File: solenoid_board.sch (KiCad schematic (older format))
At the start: 30 parts, among them J2 MCU_LEFT_LEGS, J3 MCU_RIGHT_LEGS

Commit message: Changed resistor footprints, changed resistor supplier. Still need to route wires.
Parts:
- R330, R331, R332, R333, R334, R335, R336, R337, R338: footprint Resistor_SMD:R_2010_5025Metric_Pad1.52x2.65mm_HandSolder -> Resistor_THT:R_Axial_DIN0309_L9.0mm_D3.2mm_P20.32mm_Horizontal
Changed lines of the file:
@@
 F 0 "R330" V 9000 850 50  0000 C CNN
 F 1 "330" V 9016 850 50  0001 C CNN
-F 2 "Resistor_SMD:R_2010_5025Metric_Pad1.52x2.65mm_HandSolder" V 8830 850 50  0001 C CNN
+F 2 "Resistor_THT:R_Axial_DIN0309_L9.0mm_D3.2mm_P20.32mm_Horizontal" V 8830 850 50  0001 C CNN
 F 3 "~" H 8900 850 50  0001 C CNN
 	1    8900 850
@@
 F 0 "R331" V 9000 1100 50  0000 C CNN
 F 1 "330" V 9016 1100 50  0001 C CNN
-F 2 "Resistor_SMD:R_2010_5025Metric_Pad1.52x2.65mm_HandSolder" V 8830 1100 50  0001 C CNN
+F 2 "Resistor_THT:R_Axial_DIN0309_L9.0mm_D3.2mm_P20.32mm_Horizontal" V 8830 1100 50  0001 C CNN
 F 3 "~" H 8900 1100 50  0001 C CNN
 	1    8900 1100
@@
 F 0 "R332" V 9000 1350 50  0000 C CNN
 F 1 "330" V 9016 1350 50  0001 C CNN
-F 2 "Resistor_SMD:R_2010_5025Metric_Pad1.52x2.65mm_HandSolder" V 8830 1350 50  0001 C CNN
+F 2 "Resistor_THT:R_Axial_DIN0309_L9.0mm_D3.2mm_P20.32mm_Horizontal" V 8830 1350 50  0001 C CNN
 F 3 "~" H 8900 1350 50  0001 C CNN
 	1    8900 1350
@@
 F 0 "R333" V 9000 1600 50  0000 C CNN
 F 1 "R" V 9016 1600 50  0001 C CNN
-F 2 "Resistor_SMD:R_2010_5025Metric_Pad1.52x2.65mm_HandSolder" V 8830 1600 50  0001 C CNN
+F 2 "Resistor_THT:R_Axial_DIN0309_L9.0mm_D3.2mm_P20.32mm_Horizontal" V 8830 1600 50  0001 C CNN
 F 3 "~" H 8900 1600 50  0001 C CNN
 	1    8900 1600
@@
 F 0 "R334" V 9000 1850 50  0000 C CNN
 F 1 "R" V 9016 1850 50  0001 C CNN
-F 2 "Resistor_SMD:R_2010_5025Metric_Pad1.52x2.65mm_HandSolder" V 8830 1850 50  0001 C CNN
+F 2 "Resistor_THT:R_Axial_DIN0309_L9.0mm_D3.2mm_P20.32mm_Horizontal" V 8830 1850 50  0001 C CNN
 F 3 "~" H 8900 1850 50  0001 C CNN
 	1    8900 1850
@@
 F 0 "R335" V 9000 2100 50  0000 C CNN
 F 1 "R" V 9016 2100 50  0001 C CNN
-F 2 "Resistor_SMD:R_2010_5025Metric_Pad1.52x2.65mm_HandSolder" V 8830 2100 50  0001 C CNN
+F 2 "Resistor_THT:R_Axial_DIN0309_L9.0mm_D3.2mm_P20.32mm_Horizontal" V 8830 2100 50  0001 C CNN
 F 3 "~" H 8900 2100 50  0001 C CNN
 	1    8900 2100
@@
 F 0 "R336" V 9000 2350 50  0000 C CNN
 F 1 "R" V 9016 2350 50  0001 C CNN
-F 2 "Resistor_SMD:R_2010_5025Metric_Pad1.52x2.65mm_HandSolder" V 8830 2350 50  0001 C CNN
+F 2 "Resistor_THT:R_Axial_DIN0309_L9.0mm_D3.2mm_P20.32mm_Horizontal" V 8830 2350 50  0001 C CNN
 F 3 "~" H 8900 2350 50  0001 C CNN
 	1    8900 2350
@@
 F 0 "R337" V 9000 2600 50  0000 C CNN
 F 1 "R" V 9016 2600 50  0001 C CNN
-F 2 "Resistor_SMD:R_2010_5025Metric_Pad1.52x2.65mm_HandSolder" V 8830 2600 50  0001 C CNN
+F 2 "Resistor_THT:R_Axial_DIN0309_L9.0mm_D3.2mm_P20.32mm_Horizontal" V 8830 2600 50  0001 C CNN
 F 3 "~" H 8900 2600 50  0001 C CNN
 	1    8900 2600
@@
 F 0 "R338" V 9000 2900 50  0000 C CNN
 F 1 "R" V 9016 2900 50  0001 C CNN
-F 2 "Resistor_SMD:R_2010_5025Metric_Pad1.52x2.65mm_HandSolder" V 8830 2900 50  0001 C CNN
+F 2 "Resistor_THT:R_Axial_DIN0309_L9.0mm_D3.2mm_P20.32mm_Horizontal" V 8830 2900 50  0001 C CNN
 F 3 "~" H 8900 2900 50  0001 C CNN
 	1    8900 2900

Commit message: Rearranged Component Geometry, switched out Transciever Resistor footprints, Routed Some wires.
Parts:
- R10, R11: footprint Resistor_SMD:R_2010_5025Metric_Pad1.52x2.65mm_HandSolder -> Resistor_THT:R_Axial_DIN0309_L9.0mm_D3.2mm_P20.32mm_Horizontal
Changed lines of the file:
@@
 F 0 "R11" V 2950 3200 50  0000 C CNN
 F 1 "10" V 2750 3200 50  0001 C CNN
-F 2 "Resistor_SMD:R_2010_5025Metric_Pad1.52x2.65mm_HandSolder" V 2780 3200 50  0001 C CNN
+F 2 "Resistor_THT:R_Axial_DIN0309_L9.0mm_D3.2mm_P20.32mm_Horizontal" V 2780 3200 50  0001 C CNN
 F 3 "~" H 2850 3200 50  0001 C CNN
 	1    2850 3200
@@
 F 0 "R10" V 2750 2950 50  0000 C CNN
 F 1 "10" V 2734 2950 50  0001 C CNN
-F 2 "Resistor_SMD:R_2010_5025Metric_Pad1.52x2.65mm_HandSolder" V 2780 2950 50  0001 C CNN
+F 2 "Resistor_THT:R_Axial_DIN0309_L9.0mm_D3.2mm_P20.32mm_Horizontal" V 2780 2950 50  0001 C CNN
 F 3 "~" H 2850 2950 50  0001 C CNN
 	1    2850 2950

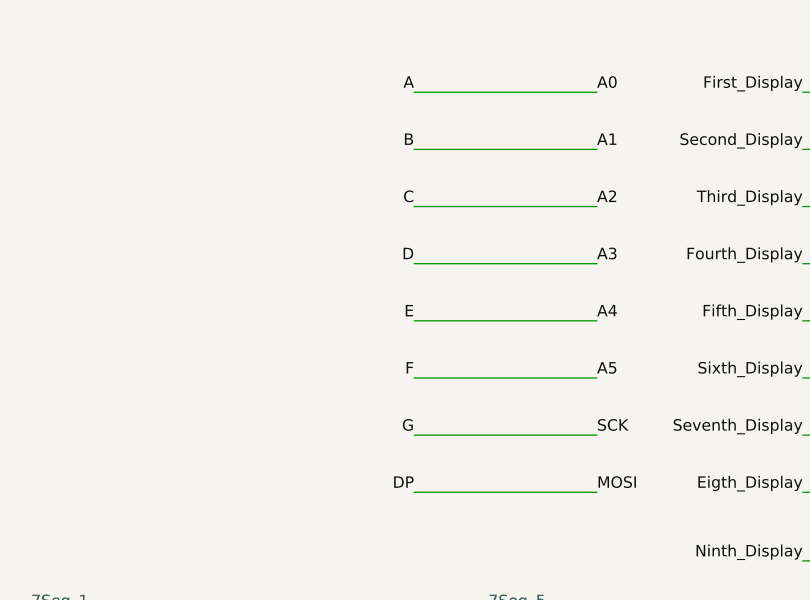
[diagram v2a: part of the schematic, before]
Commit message: Finished Routing and generated new .gbr files. I am unsatisfied with the size of the board, and the geometry may need to be moved around to allow ball count to be displayed underneath the score.
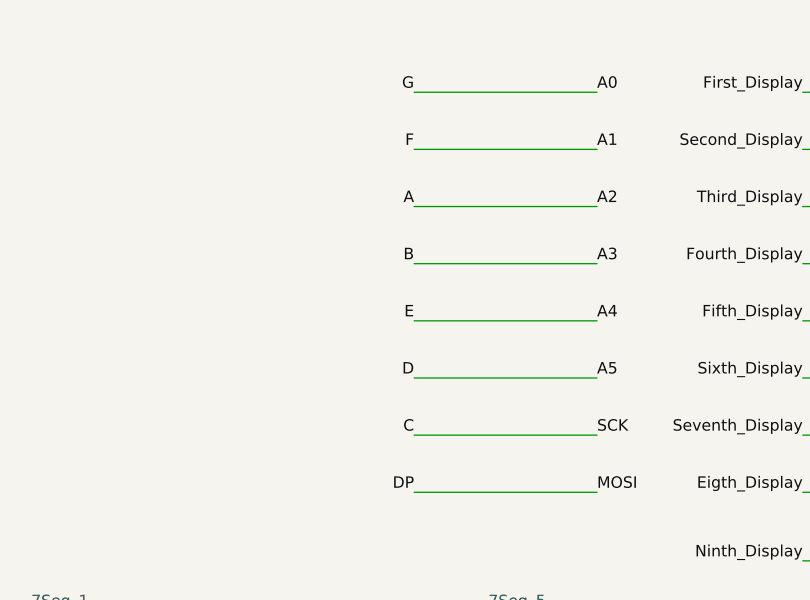
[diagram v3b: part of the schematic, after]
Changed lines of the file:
@@
 Ninth_Display
 Text Label 6800 850  2    50   ~ 0
+G
+Text Label 6800 1100 2    50   ~ 0
+F
+Text Label 6800 1350 2    50   ~ 0
 A
-Text Label 6800 1100 2    50   ~ 0
+Text Label 6800 1600 2    50   ~ 0
 B
-Text Label 6800 1350 2    50   ~ 0
-C
-Text Label 6800 1600 2    50   ~ 0
-D
 Text Label 6800 1850 2    50   ~ 0
 E
 Text Label 6800 2100 2    50   ~ 0
-F
+D
 Text Label 6800 2350 2    50   ~ 0
-G
+C
 Text Label 6800 2600 2    50   ~ 0
 DP

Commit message: Changed BOM, changed Schematic symbols/footprints. Still need to add mosfets and ICs.
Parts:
- removed +5V_IN1: MCU_PWR_Supply, TerminalBlock:TerminalBlock_bornier-2_P5.08mm, symbol Connector:Screw_Terminal_01x02
- removed 7Seg_5, 7Seg_6, 7Seg_7, 7Seg_8, 7Seg_9: Conn_02x05_Top_Bottom, Display_7Segment:7SegmentLED_LTS6760_LTS6780, symbol Connector_Generic:Conn_02x05_Top_Bottom
- removed GND1: Conn_01x01_Male, Connector_PinHeader_2.54mm:PinHeader_1x01_P2.54mm_Vertical, symbol Connector:Conn_01x01_Male
- removed RJ0, RJ1: RJ45, Connector_RJ:RJ45_Amphenol_54602-x08_Horizontal, symbol Connector:RJ45
- added +5VIN, COMMS0, COMMS1: Conn_01x02, Connector_PinHeader_2.54mm:PinHeader_1x02_P2.54mm_Vertical, symbol Connector_Generic:Conn_01x02
- added GND1: Conn_01x01, symbol Connector_Generic:Conn_01x01
- 7Seg_2, 7Seg_3, 7Seg_4: footprint Display_7Segment:7SegmentLED_LTS6760_LTS6780 -> digikey-footprints:DIP-10_W10.16mm
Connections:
- net labels removed: RJ45_4, RJ45_5
- wire segments 44 -> 46
- no-connect marks 16 -> 4

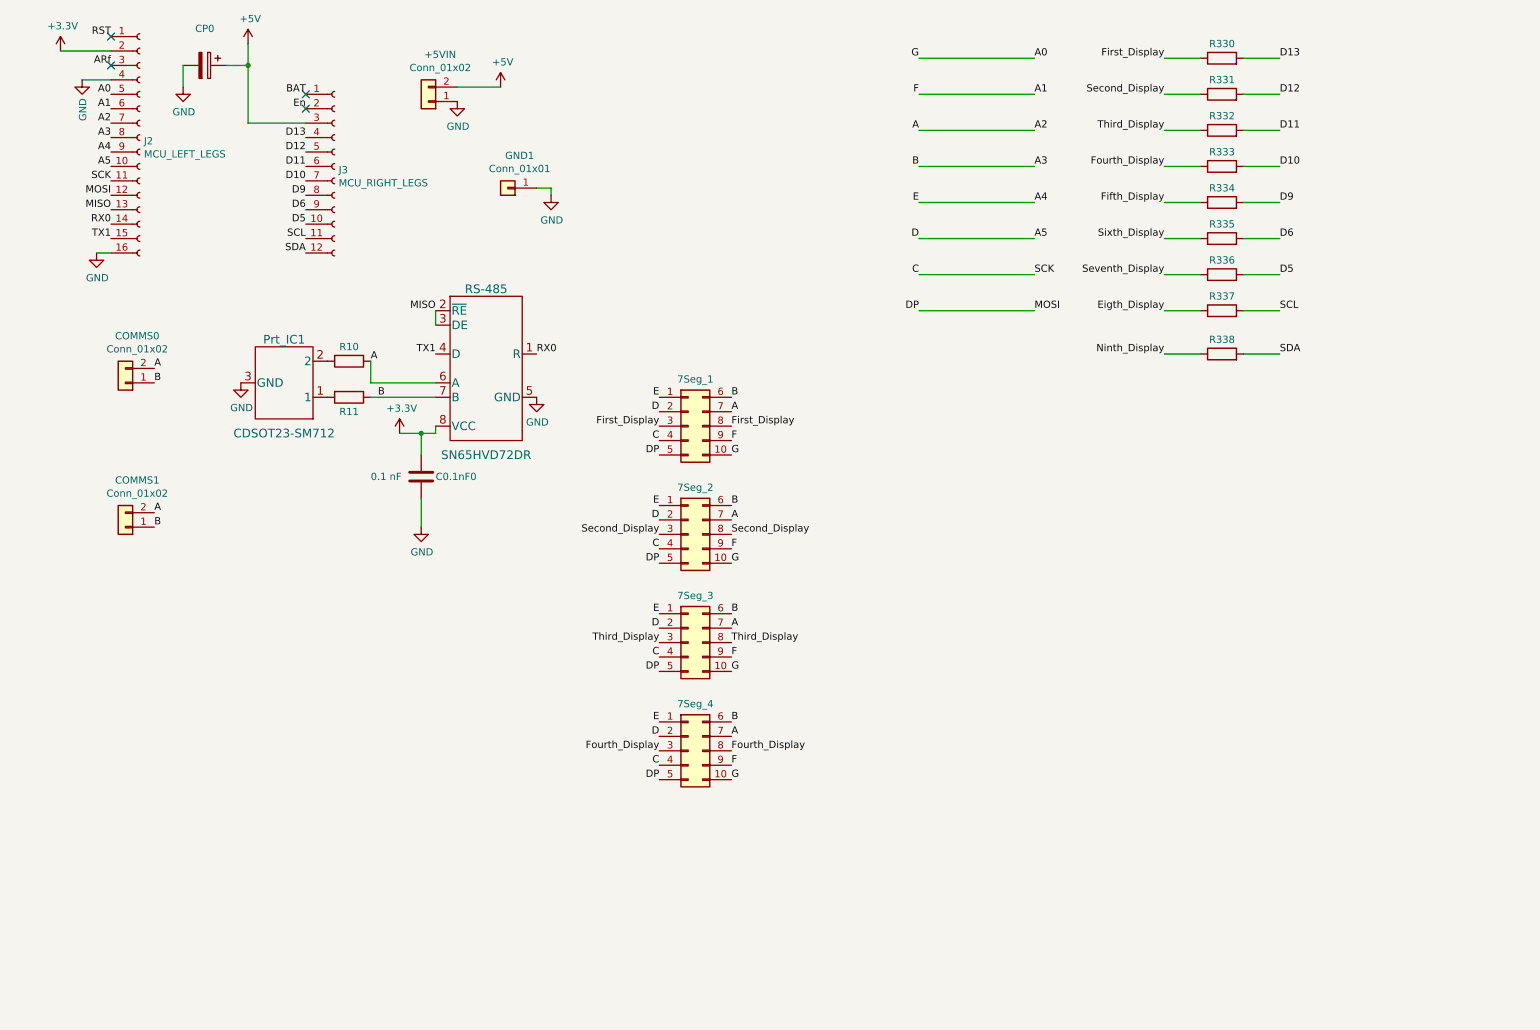
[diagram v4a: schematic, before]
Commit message: Major revisions occurred to the Schematic. Sourced 7-Segment display and MosFETs.
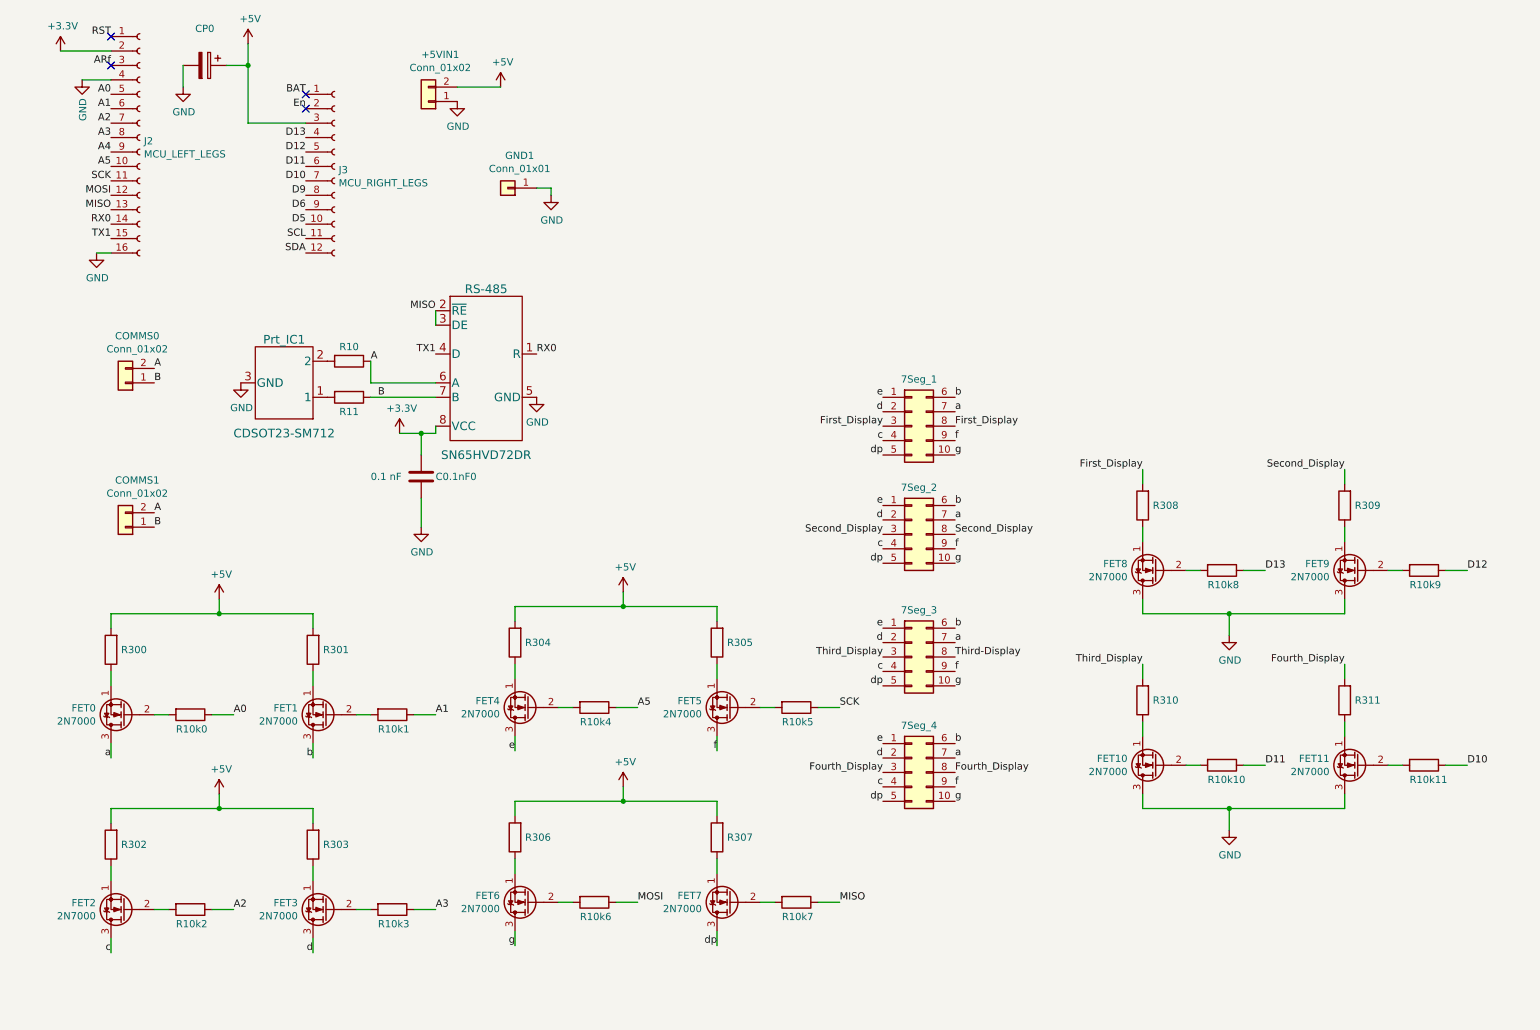
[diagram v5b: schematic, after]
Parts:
- removed R330, R331, R332: 330, Resistor_THT:R_Axial_DIN0309_L9.0mm_D3.2mm_P20.32mm_Horizontal, symbol Device:R
- removed R333, R334, R335, R336, R337, R338: R, Resistor_THT:R_Axial_DIN0309_L9.0mm_D3.2mm_P20.32mm_Horizontal, symbol Device:R
- added FET0, FET1, FET10, FET11, FET2, FET3, FET4, FET5, FET6, FET7, FET8, FET9: 2N7000, Package_TO_SOT_THT:TO-92_Inline, symbol Transistor_FET:2N7000
- added R10k0, R10k1, R10k10, R10k11, R10k2, R10k3, R10k4, R10k5, R10k6, R10k7, R10k8, R10k9: 10k, Resistor_THT:R_Axial_DIN0204_L3.6mm_D1.6mm_P5.08mm_Vertical, symbol Device:R
- added R300, R301, R302, R303, R304, R305, R306, R307, R308, R309, R310, R311: 300, Resistor_THT:R_Axial_DIN0204_L3.6mm_D1.6mm_P5.08mm_Vertical, symbol Device:R
- 7Seg_1: footprint Display_7Segment:7SegmentLED_LTS6760_LTS6780 -> Kingbright_10-DinDisplay:SC10-21SRWA
- 7Seg_2, 7Seg_3, 7Seg_4: footprint digikey-footprints:DIP-10_W10.16mm -> Kingbright_10-DinDisplay:SC10-21SRWA
- GND1: footprint (none) -> Connector_PinHeader_2.54mm:PinHeader_1x01_P2.54mm_Vertical
- renumbered +5VIN to +5VIN1
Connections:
- net +5V: now also R300.2, R301.2, R302.2, R303.2, R304.2, R305.2, R306.2, R307.2
- net A: no longer 7Seg_1.7 (Pin_7), 7Seg_2.7 (Pin_7), 7Seg_3.7 (Pin_7), 7Seg_4.7 (Pin_7), J2.7 (Pin_7)
- net A0: now also R10k0.1; no longer 7Seg_1.10 (Pin_10), 7Seg_2.10 (Pin_10), 7Seg_3.10 (Pin_10), 7Seg_4.10 (Pin_10)
- net A1: now also R10k1.1; no longer 7Seg_1.9 (Pin_9), 7Seg_2.9 (Pin_9), 7Seg_3.9 (Pin_9), 7Seg_4.9 (Pin_9)
- net A3: now also R10k3.1; no longer 7Seg_1.6 (Pin_6), 7Seg_2.6 (Pin_6), 7Seg_3.6 (Pin_6), 7Seg_4.6 (Pin_6), COMMS0.1 (Pin_1), COMMS1.1 (Pin_1), R11.1, RS-485.7 (B)
- net A4: no longer 7Seg_1.1 (Pin_1), 7Seg_2.1 (Pin_1), 7Seg_3.1 (Pin_1), 7Seg_4.1 (Pin_1)
- net A5: now also R10k4.1; no longer 7Seg_1.2 (Pin_2), 7Seg_2.2 (Pin_2), 7Seg_3.2 (Pin_2), 7Seg_4.2 (Pin_2)
- net D10: now also R10k11.1
- net D11: now also R10k10.1
- net D12: now also R10k9.1
- net D13: now also R10k8.1
- net First_Display: now also R308.2
- net Fourth_Display: now also R311.2
- net GND: now also FET10.3 (D), FET11.3 (D), FET8.3 (D), FET9.3 (D)
- net MISO: now also R10k7.1
- net Second_Display: now also R309.2
- net Third_Display: now also R310.2; no longer 7Seg_3.8 (Pin_8)
- net C renamed c
- net c: now also FET2.3 (D); no longer J2.11 (Pin_11)
- net DP renamed dp
- net dp: now also FET7.3 (D); no longer J2.12 (Pin_12)
- new net: FET0.1 (S), R300.1
- new net: FET0.2 (G), R10k0.2
- new net: FET1.1 (S), R301.1
- new net: FET1.2 (G), R10k1.2
- new net: FET2.1 (S), R302.1
- new net: FET2.2 (G), R10k2.2
- new net: FET3.1 (S), R303.1
- new net: FET3.2 (G), R10k3.2
- new net: FET4.1 (S), R304.1
- new net: FET4.2 (G), R10k4.2
- new net: FET5.1 (S), R305.1
- new net: FET5.2 (G), R10k5.2
- new net: FET6.1 (S), R306.1
- new net: FET6.2 (G), R10k6.2
- new net: FET7.1 (S), R307.1
- new net: FET7.2 (G), R10k7.2
- new net: FET8.1 (S), R308.1
- new net: FET8.2 (G), R10k8.2
- new net: FET9.1 (S), R309.1
- new net: FET9.2 (G), R10k9.2
- new net: FET10.1 (S), R310.1
- new net: FET10.2 (G), R10k10.2
- new net: FET11.1 (S), R311.1
- new net: FET11.2 (G), R10k11.2
- new net A2: J2.7 (Pin_7), R10k2.1
- new net B: COMMS0.1 (Pin_1), COMMS1.1 (Pin_1), R11.1, RS-485.7 (B)
- new net MOSI: J2.12 (Pin_12), R10k6.1
- new net SCK: J2.11 (Pin_11), R10k5.1
- new net Third-Display: 7Seg_3.8 (Pin_8)
- new net a: 7Seg_1.7 (Pin_7), 7Seg_2.7 (Pin_7), 7Seg_3.7 (Pin_7), 7Seg_4.7 (Pin_7), FET0.3 (D)
- new net b: 7Seg_1.6 (Pin_6), 7Seg_2.6 (Pin_6), 7Seg_3.6 (Pin_6), 7Seg_4.6 (Pin_6), FET1.3 (D)
- new net d: 7Seg_1.2 (Pin_2), 7Seg_2.2 (Pin_2), 7Seg_3.2 (Pin_2), 7Seg_4.2 (Pin_2), FET3.3 (D)
- new net e: 7Seg_1.1 (Pin_1), 7Seg_2.1 (Pin_1), 7Seg_3.1 (Pin_1), 7Seg_4.1 (Pin_1), FET4.3 (D)
- new net f: 7Seg_1.9 (Pin_9), 7Seg_2.9 (Pin_9), 7Seg_3.9 (Pin_9), 7Seg_4.9 (Pin_9), FET5.3 (D)
- new net g: 7Seg_1.10 (Pin_10), 7Seg_2.10 (Pin_10), 7Seg_3.10 (Pin_10), 7Seg_4.10 (Pin_10), FET6.3 (D)
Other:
- moved on the sheet: 7Seg_1
